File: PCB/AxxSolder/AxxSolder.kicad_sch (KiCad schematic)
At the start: 95 parts, among them IC1 LTC4440AHMS8E-5#PBF, IC2 STM32G431KBT6, IC3 TMP236AQDBZRQ1, IC4 OPA2333AIDRBR, IC5 STM32G431KBT6, IC6 TPS54302DDCR, J1 Conn_01x07_Male, J4 Conn_01x07_Male, Q2 2N7002NXAKR, U1 PEC11L-4220F-S0015, U2 BSC014N04LS

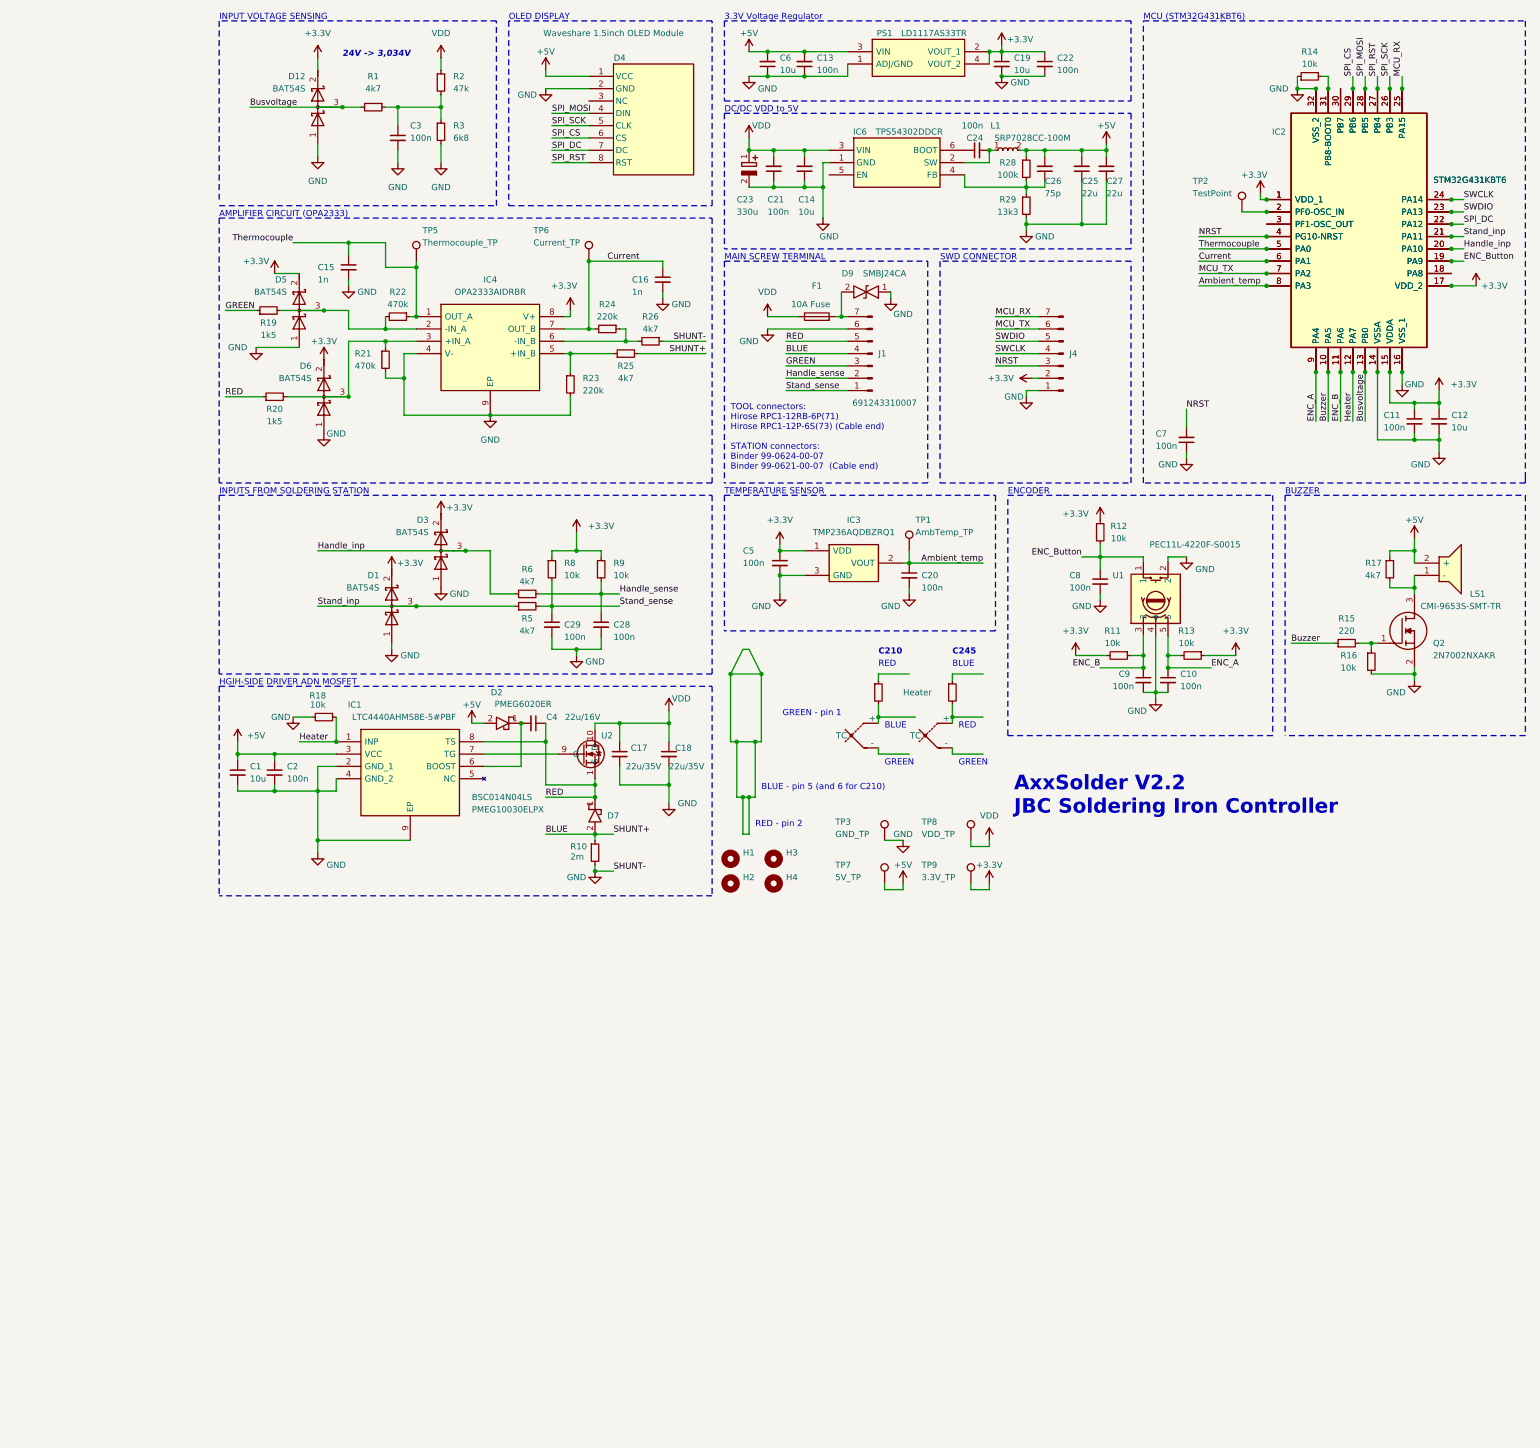
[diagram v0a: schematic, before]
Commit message: add libraries and import components for USB firmware upload and USB PD
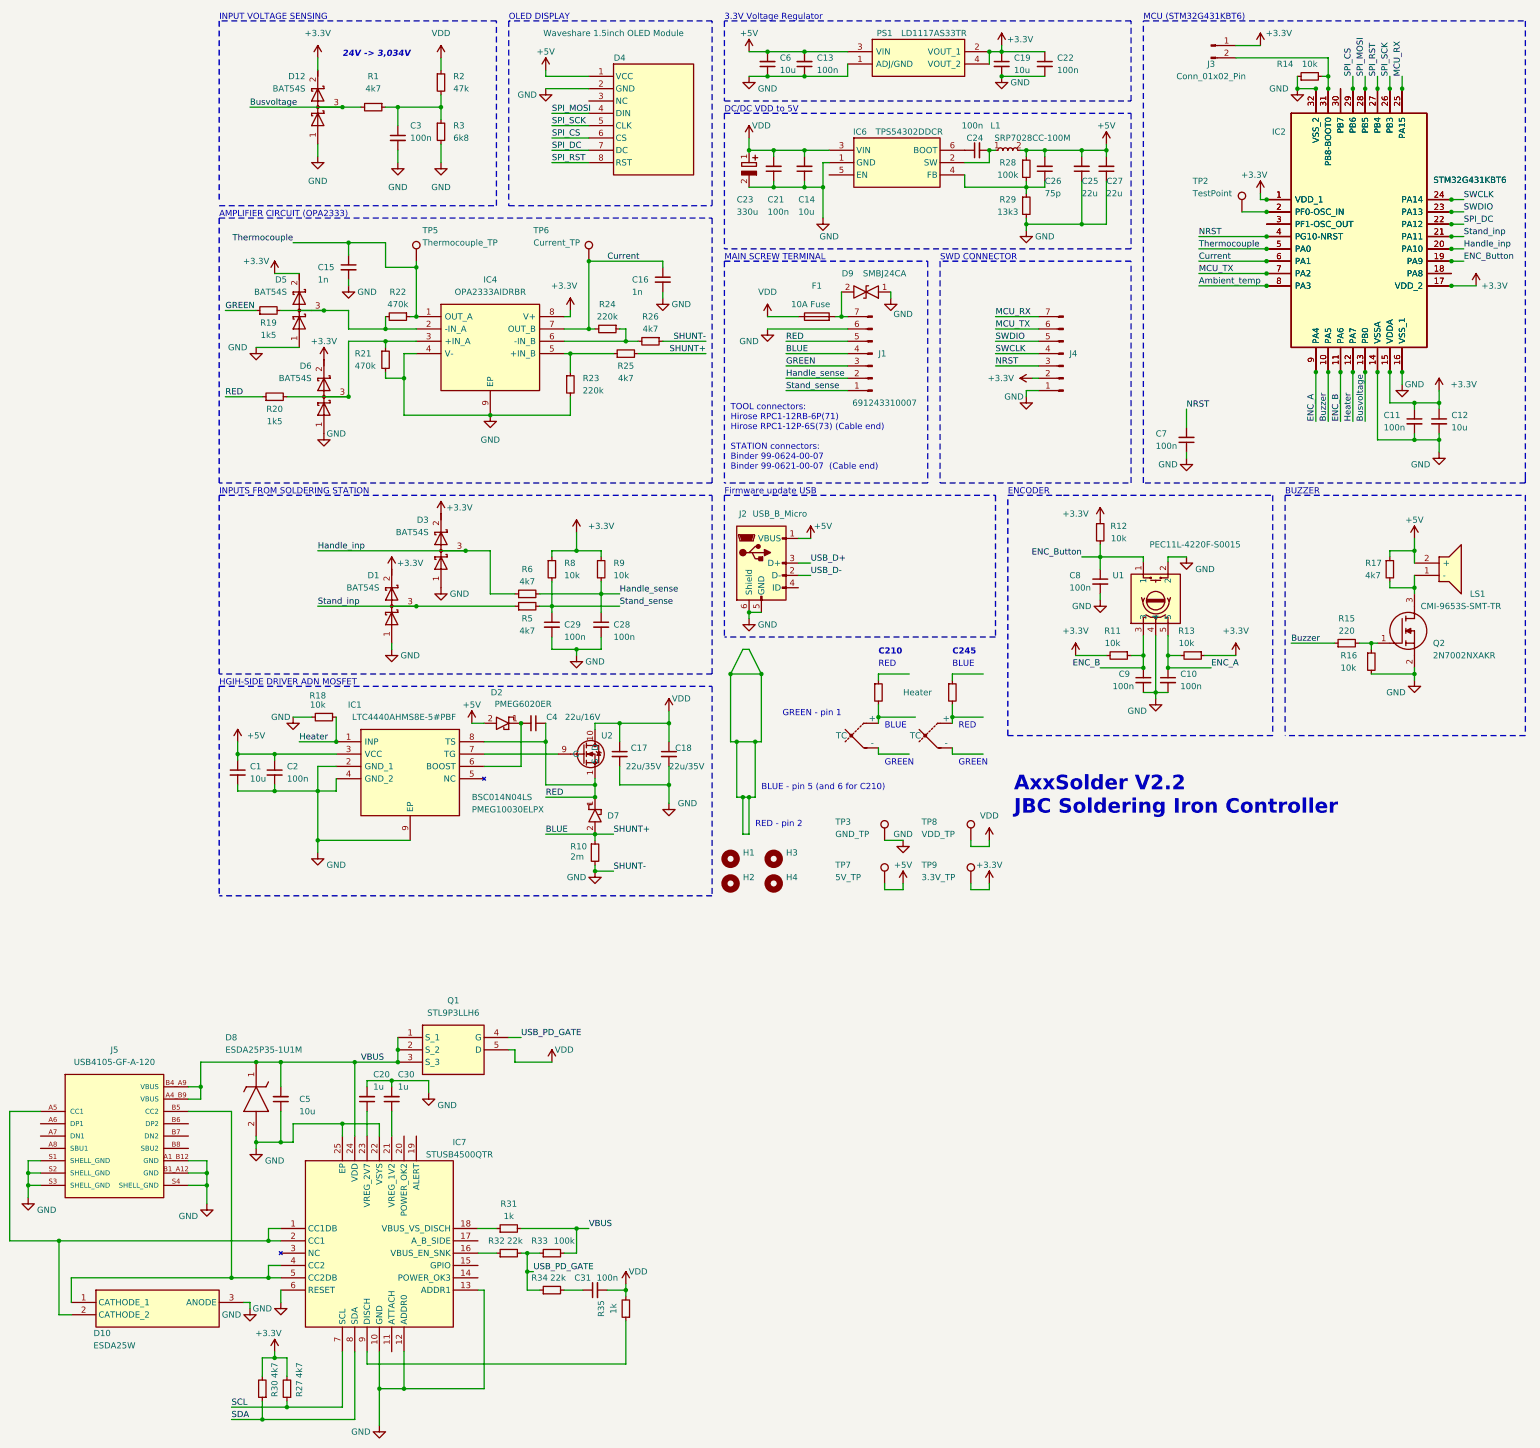
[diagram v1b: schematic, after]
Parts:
- removed IC3: TMP236AQDBZRQ1, TMP236AQDBZRQ1:SOT95P237X112-3N, symbol TMP236AQDBZRQ1:TMP236AQDBZRQ1
- removed TP1: AmbTemp_TP, TestPoint:TestPoint_THTPad_D1.0mm_Drill0.5mm, symbol Connector:TestPoint
- added C30: 1u, Capacitor_SMD:C_0805_2012Metric, symbol Device:C_Small
- added C31: 100n, Capacitor_SMD:C_0805_2012Metric, symbol Device:C_Small
- added D10: ESDA25W, ESDA25W:SOT65P210X110-3N, symbol ESDA25W:ESDA25W
- added D8: ESDA25P35-1U1M, ESDA25P35-1U1M:ESDA25P351U1M, symbol ESDA25P35-1U1M:ESDA25P35-1U1M
- added IC7: STUSB4500QTR, STUSB4500QTR:QFN50P400X400X100-25N-D, symbol STUSB4500QTR:STUSB4500QTR
- added J2: USB_B_Micro, USB3140-30-0230-1-C_REVE1:GCT_USB3140-30-0230-1-C_REVE1, symbol Connector:USB_B_Micro
- added J3: Conn_01x02_Pin, Connector_PinHeader_2.54mm:PinHeader_1x02_P2.54mm_Vertical, symbol Connector:Conn_01x02_Pin
- added J5: USB4105-GF-A-120, USB4105-GF-A:GCT_USB4105-GF-A-120, symbol USB4105-GF-A-120:USB4105-GF-A-120
- added Q1: STL9P3LLH6, STL9P3LLH6:STL20N6F7, symbol STL9P3LLH6:STL9P3LLH6
- added R27, R30: 4k7, Resistor_SMD:R_0805_2012Metric, symbol Device:R_Small
- added R31, R35: 1k, Resistor_SMD:R_0805_2012Metric, symbol Device:R_Small
- added R32, R34: 22k, Resistor_SMD:R_0805_2012Metric, symbol Device:R_Small
- added R33: 100k, Resistor_SMD:R_0805_2012Metric, symbol Device:R_Small
- C20: value 100n -> 1u
- C5: value 100n -> 10u
- D9: footprint DIOM5436X261N -> SMBJ24CA:DIOM5436X261N
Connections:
- net +3.3V: now also J3.1 (Pin_1), R27.2, R30.2; no longer C5.1
- net +5V: now also J2.1 (VBUS)
- net Ambient_temp: no longer C20.1
- net GND: now also C5.1, C30.2, D10.3 (ANODE), D8.2 (A), IC7.10 (GND), IC7.12 (ADDR0), IC7.13 (ADDR1), IC7.22 (VSYS), IC7.25 (EP), IC7.6 (RESET), J2.5 (GND), J2.6 (Shield), J5.A1_B12 (GND), J5.B1_A12 (GND), J5.S1 (SHELL_GND), J5.S2 (SHELL_GND), J5.S3 (SHELL_GND), J5.S4 (SHELL_GND); no longer C5.2
- net VDD: now also C31.2, Q1.5 (D), R35.2
- net at IC2.31 (PB8-BOOT0), IC5.31 (PB8-BOOT0), R14.2: now also J3.2 (Pin_2)
- new net: C30.1, IC7.21 (VREG_1V2)
- new net: D10.1 (CATHODE_1), IC7.4 (CC2), IC7.5 (CC2DB), J5.B5 (CC2)
- new net: D10.2 (CATHODE_2), IC7.1 (CC1DB), IC7.2 (CC1), J5.A5 (CC1)
- new net: C31.1, R34.2
- new net: IC7.16 (VBUS_EN_SNK), R32.1
- new net: IC7.9 (DISCH), R35.1
- new net: C20.1, IC7.23 (VREG_2V7)
- new net: IC7.18 (VBUS_VS_DISCH), R31.1
- new net SCL: IC7.7 (SCL), R27.1
- new net SDA: IC7.8 (SDA), R30.1
- new net USB_D+: J2.3 (D+)
- new net USB_D-: J2.2 (D-)
- new net USB_PD_GATE: Q1.4 (G), R32.2, R33.1, R34.1
- new net VBUS: C5.2, D8.1 (K), IC7.24 (VDD), J5.A4_B9 (VBUS), J5.B4_A9 (VBUS), Q1.1 (S_1), Q1.2 (S_2), Q1.3 (S_3), R31.2, R33.2
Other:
- note added: "Firmware update USB"
- note removed: "TEMPERATURE SENSOR"

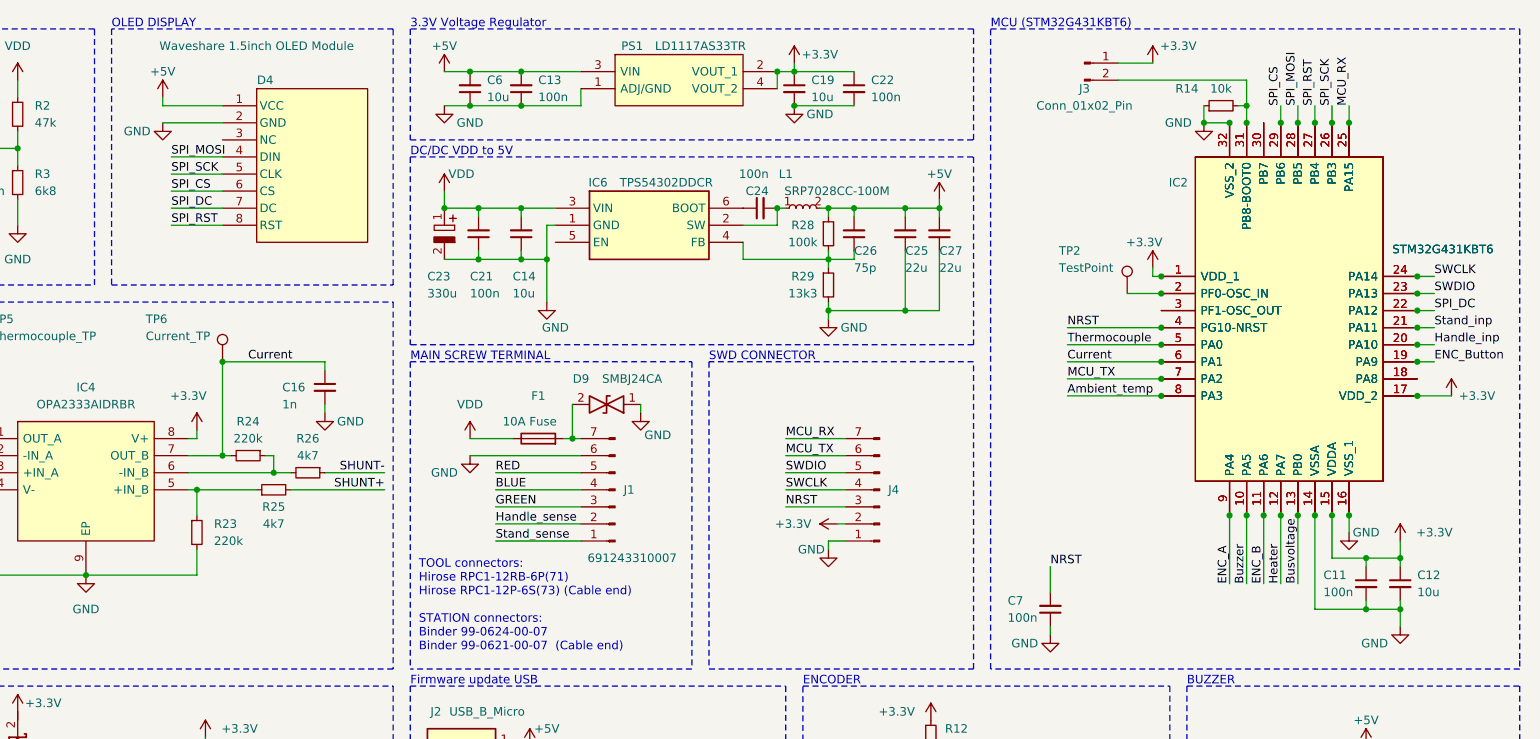
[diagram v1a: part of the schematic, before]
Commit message: update for USB support
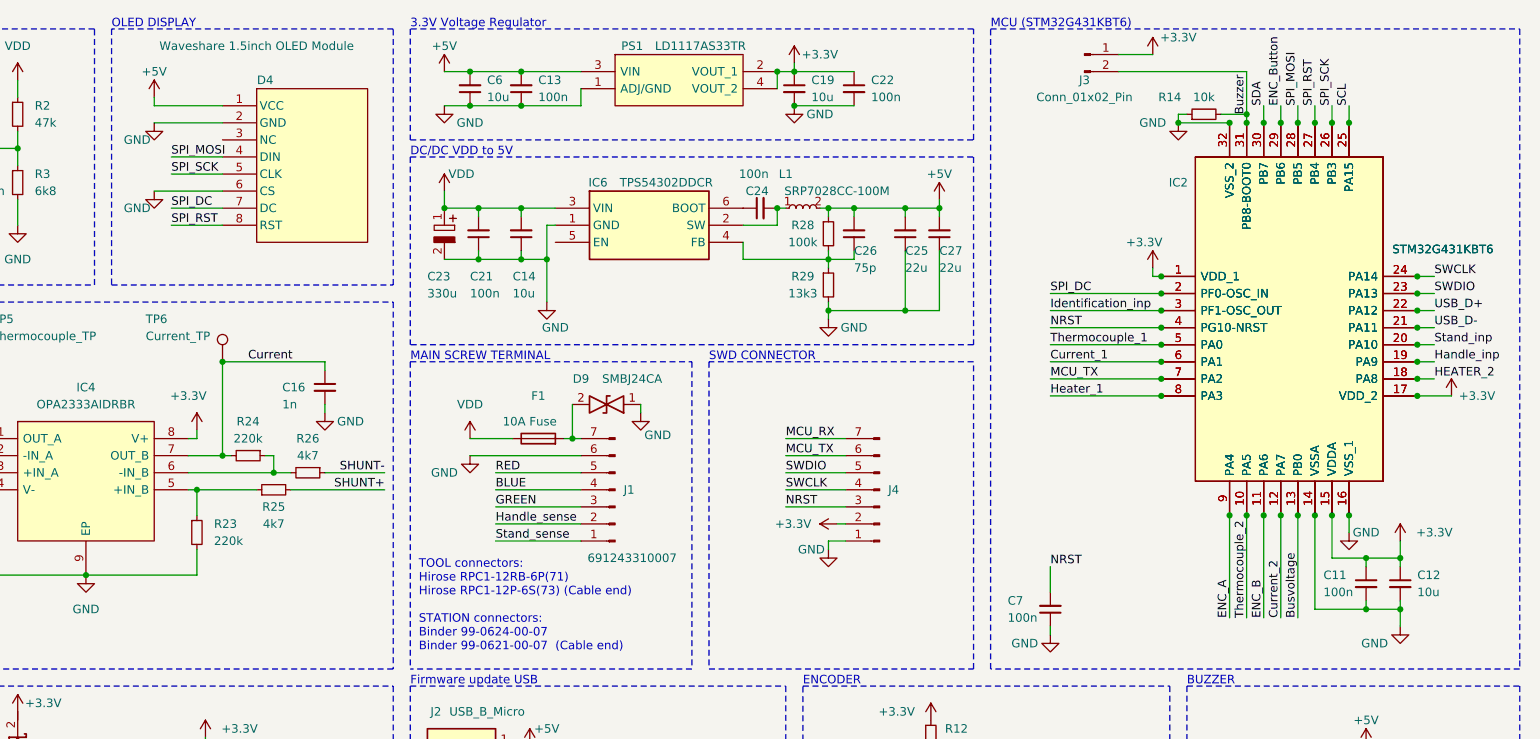
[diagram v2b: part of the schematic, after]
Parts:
- removed TP2: TestPoint, TestPoint:TestPoint_Pad_D1.0mm, symbol Connector:TestPoint
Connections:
- net Buzzer: now also IC2.31 (PB8-BOOT0), IC5.31 (PB8-BOOT0), J3.2 (Pin_2), R14.2; no longer IC2.10 (PA5), IC5.10 (PA5)
- net Current: no longer IC2.6 (PA1), IC5.6 (PA1)
- net ENC_Button: now also IC2.29 (PB6), IC5.29 (PB6); no longer IC2.19 (PA9), IC5.19 (PA9)
- net GND: now also D4.6 (CS)
- net Handle_inp: now also IC2.19 (PA9), IC5.19 (PA9); no longer IC2.20 (PA10), IC5.20 (PA10)
- net Heater: no longer IC2.12 (PA7), IC5.12 (PA7)
- net MCU_RX: no longer IC2.25 (PA15), IC5.25 (PA15)
- net SCL: now also IC2.25 (PA15), IC5.25 (PA15)
- net SDA: now also IC2.30 (PB7), IC5.30 (PB7)
- net SPI_DC: now also IC2.2 (PF0-OSC_IN), IC5.2 (PF0-OSC_IN); no longer IC2.22 (PA12), IC5.22 (PA12)
- net Stand_inp: now also IC2.20 (PA10), IC5.20 (PA10); no longer IC2.21 (PA11), IC5.21 (PA11)
- net Thermocouple: no longer IC2.5 (PA0), IC5.5 (PA0)
- net USB_D+: now also IC2.22 (PA12), IC5.22 (PA12)
- net USB_D-: now also IC2.21 (PA11), IC5.21 (PA11)
- net HEATER_2: now reaches IC2.18 (PA8), IC5.18 (PA8)
- net Identification_inp: now reaches IC2.3 (PF1-OSC_OUT), IC5.3 (PF1-OSC_OUT)
- net Ambient_temp renamed Heater_1
- removed net SPI_CS: D4.6 (CS), IC2.29 (PB6), IC5.29 (PB6)
- new net Current_1: IC2.6 (PA1), IC5.6 (PA1)
- new net Current_2: IC2.12 (PA7), IC5.12 (PA7)
- new net Thermocouple_1: IC2.5 (PA0), IC5.5 (PA0)
- new net Thermocouple_2: IC2.10 (PA5), IC5.10 (PA5)
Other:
- moved on the sheet: J3, R14

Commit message: Update to PCB
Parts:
- removed J3: Conn_01x02_Pin, Connector_PinHeader_2.54mm:PinHeader_1x02_P2.54mm_Vertical, symbol Connector:Conn_01x02_Pin
- removed J4: Conn_01x07_Male, Connector_PinSocket_2.54mm:PinSocket_1x07_P2.54mm_Vertical, symbol Connector:Conn_01x07_Male
- added D11: 1N5819HW-7-F, 1N5819HW-7-F:SOD3716X145N, symbol 1N5819HW-7-F:1N5819HW-7-F
- added D13: V7NM103-M3_I, V7NM103-M3_I:V7NM103M3I, symbol V7NM103-M3_I:V7NM103-M3_I
- added IC8: USBLC6-2P6, USBLC6-2P6:USBLC62P6, symbol USBLC6-2P6:USBLC6-2P6
- added J6: Conn_01x06_Socket, Connector_PinSocket_2.54mm:PinSocket_1x06_P2.54mm_Vertical, symbol Connector:Conn_01x06_Socket
- added S1: PTS636_SM43_SMTR_LFS, PTS636_SM43_SMTR_LFS:PTS636SM43SMTRLFS, symbol PTS636_SM43_SMTR_LFS:PTS636_SM43_SMTR_LFS
- PS1: footprint SOT230P700X190-4N -> LD1117AS33TR:SOT230P700X190-4N
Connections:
- net Current is gone; now on net Current_1: C16.1, IC4.7 (OUT_B), R24.2, TP6.1
- net Heater is gone; now on net Heater_1: IC1.1 (INP), R18.1
- net Thermocouple is gone; now on net Thermocouple_1: C15.1, IC4.1 (OUT_A), R22.1, TP5.1
- net +3.3V: now also J6.2 (Pin_2), S1.1
- net +5V: now also D11.1
- net Buzzer: now also S1.2
- net GND: now also IC8.2 (GND), J6.1 (Pin_1)
- net MCU_TX: now also J6.6 (Pin_6)
- net NRST: now also J6.3 (Pin_3)
- net SWCLK: now also J6.4 (Pin_4)
- net SWDIO: now also J6.5 (Pin_5)
- net USB_D+: now also IC8.6 (I/O1_2); no longer J2.3 (D+)
- net USB_D-: now also IC8.4 (I/O2_2); no longer J2.2 (D-)
- net VDD: now also D13.1 (K); no longer Q1.5 (D)
- new net: D11.2, IC8.5 (VBUS)
- new net: D13.2 (A), Q1.5 (D)
- new net: IC8.1 (I/O1_1), J2.3 (D+)
- new net: IC8.3 (I/O2_1), J2.2 (D-)
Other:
- note added: "AxxSolder V3.0 JBC Soldering Iron Controller"
- note removed: "AxxSolder V2.2 JBC Soldering Iron Controller"
- moved on the sheet: R14
